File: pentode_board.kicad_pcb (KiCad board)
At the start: 2 copper layers, 72 x 45 mm, 51 parts, among them P1 L_OUT, P2 L_IN, P3 GND_in, P4 15VIN, P5 R_OUT, P6 R_IN, P7 GND_in, P8 GND_in, U1 1363HVSMPS, U2 EF86, U3 TSR0.5, U4 EF86

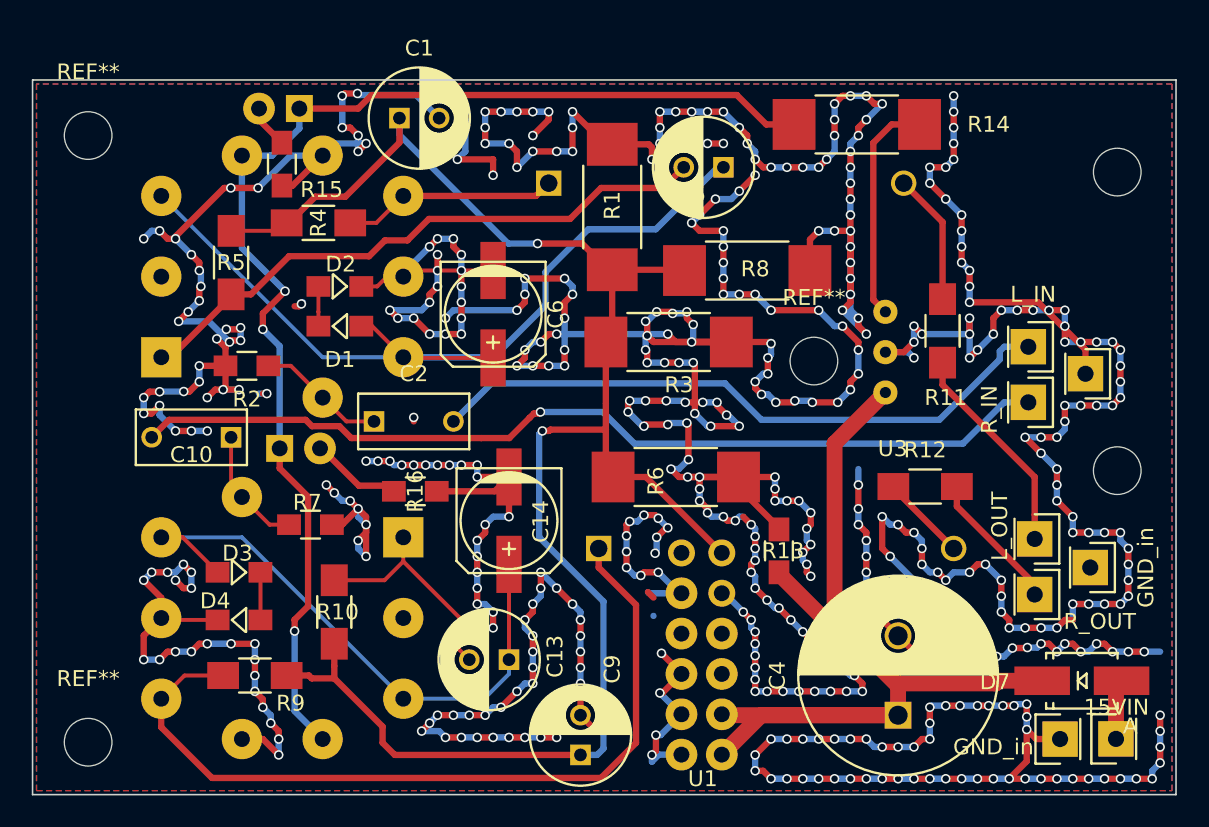
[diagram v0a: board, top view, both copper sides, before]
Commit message: After today's review: - Adjusted a few things on PCB layout - Updated and renamed BOM - Removed some junk files
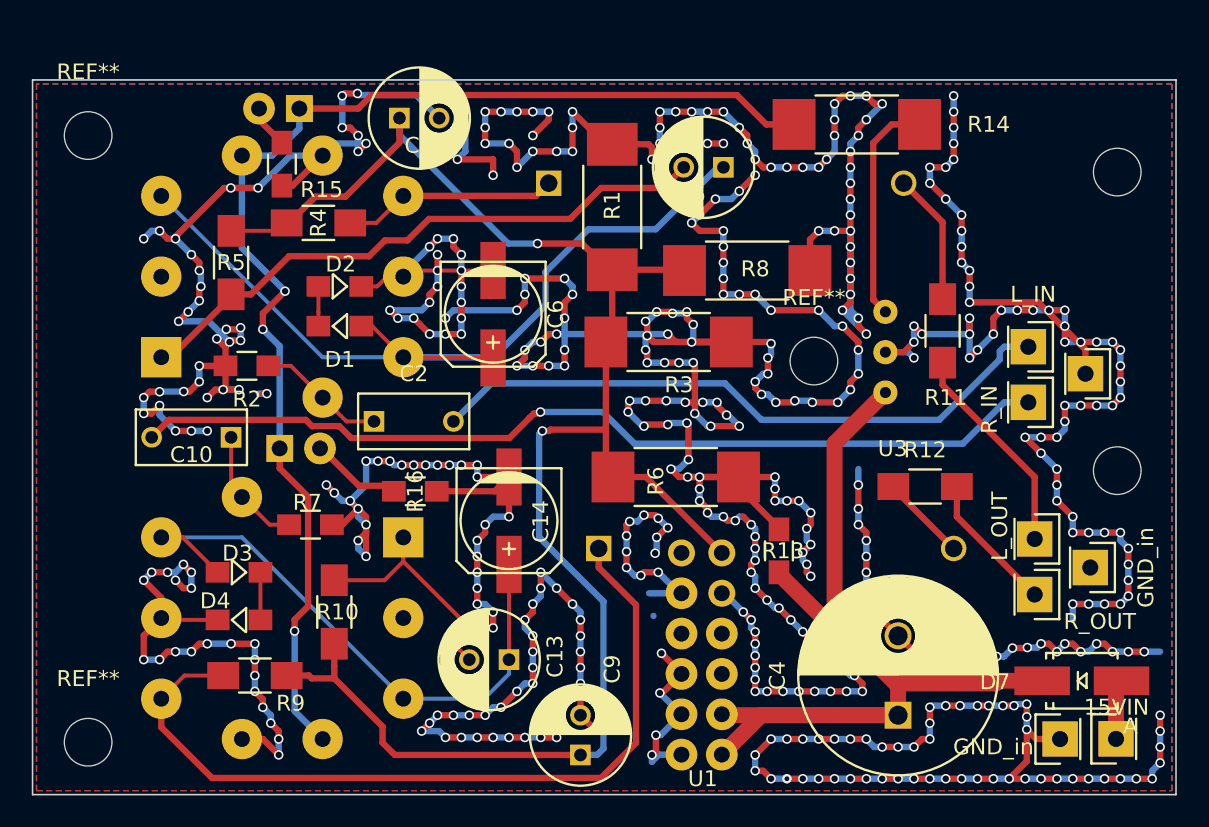
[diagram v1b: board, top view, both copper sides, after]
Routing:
- net GND: track 678.5 -> 654.4 mm, vias 487 -> 468
- net (no net): track 8.08 -> 6.71 mm, vias 5 -> 3
- net Net-(P5-Pad1): track 8.83 -> 9.48 mm
